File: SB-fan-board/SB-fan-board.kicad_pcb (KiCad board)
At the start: 2 copper layers, 51.6 x 35.1 mm, 15 parts, among them J1 FAN0, J2 FAN1, J3 NEO, J4 MAIN, U1 TPS54302

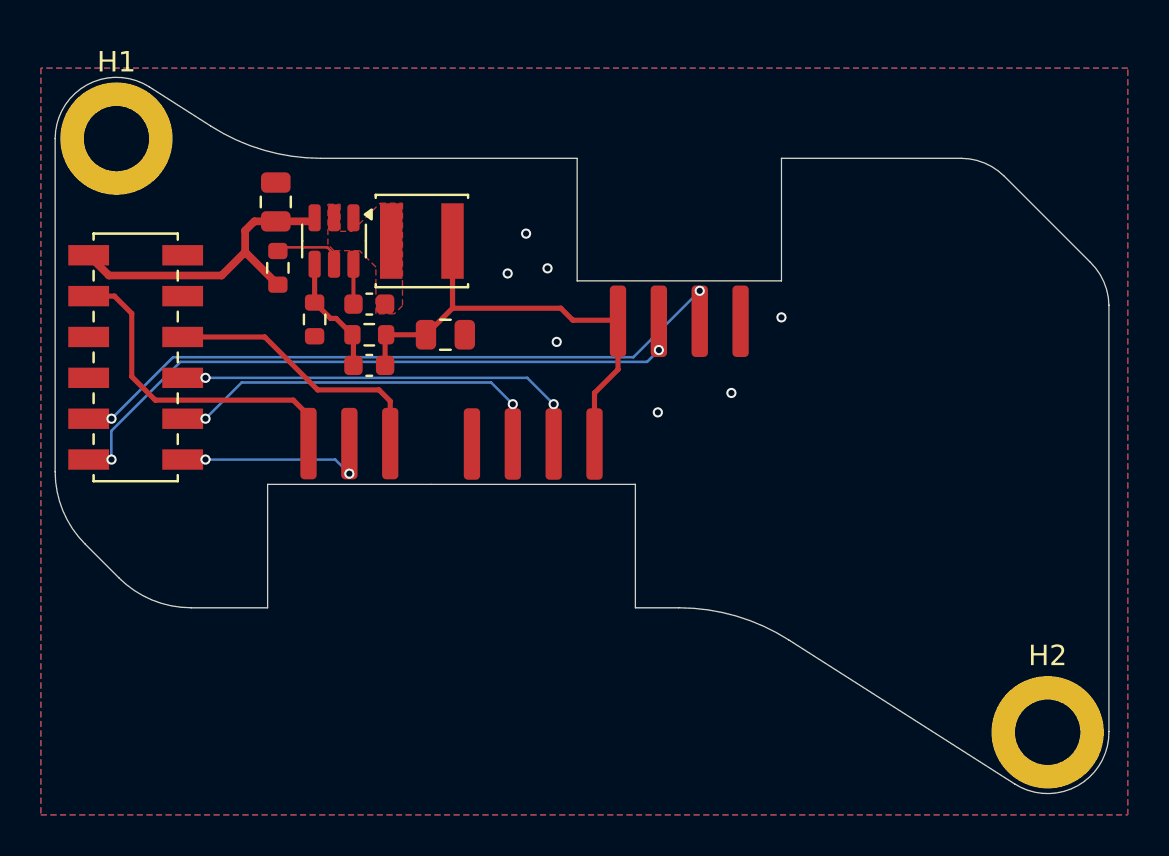
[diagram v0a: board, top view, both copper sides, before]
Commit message: mechanical: optimise installation
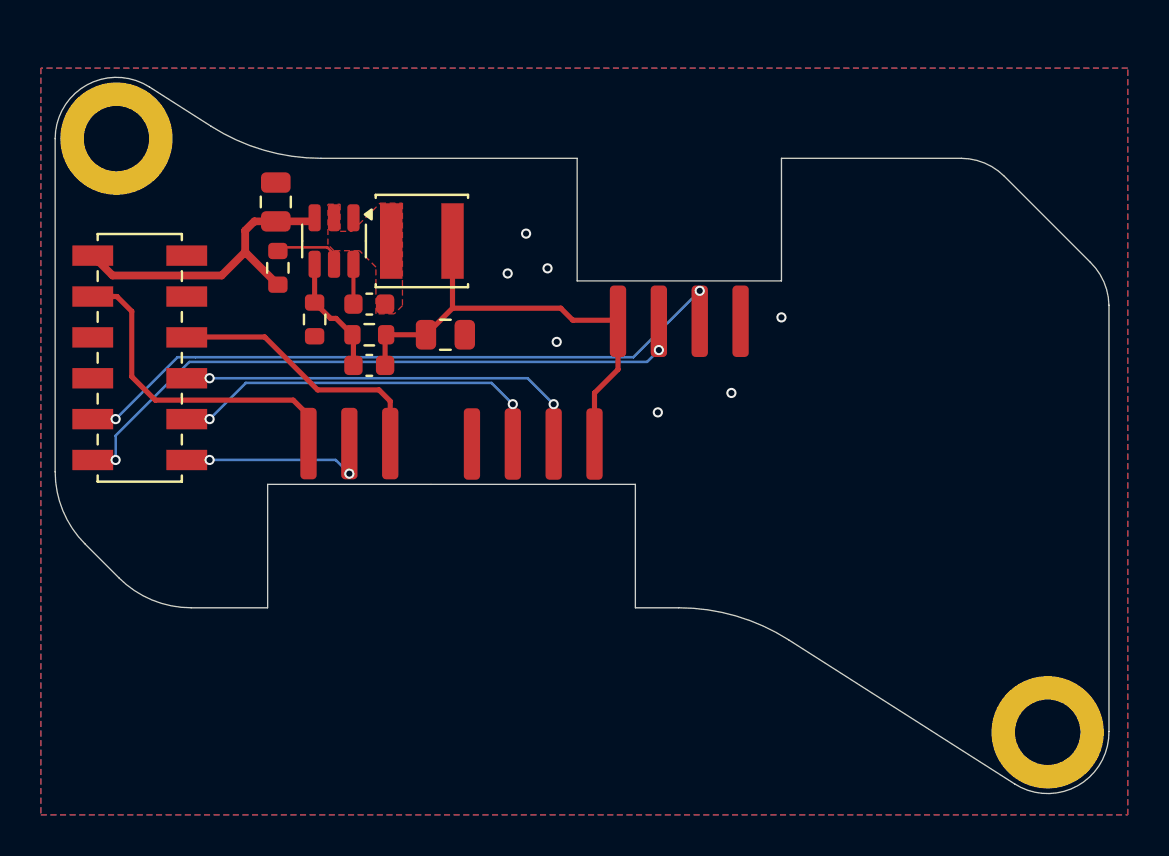
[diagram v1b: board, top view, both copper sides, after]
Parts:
- moved J4 0.20 mm to (146.3, 81.9)
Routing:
- net /FAN0_DET: track 31.0 -> 31.6 mm
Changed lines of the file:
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@@
 			(at 0 -3.75 0)
 			(layer "F.SilkS")
+			(hide yes)
 			(effects
 				(font
@@
 			(at 0 3.75 0)
 			(layer "F.Fab")
+			(hide yes)
 			(effects
 				(font
@@
 	(footprint "Library:PinSocket_2x06_P2.00mm_Vertical_SMD"
 		(layer "F.Cu")
-		(at 146.141 81.909 180)
+		(at 146.341 81.929 180)
 		(descr "surface-mounted straight socket strip, 2x06, 2.00mm pitch, double cols (from Kicad 4.0.7), script generated")
 		(tags "Surface mounted socket strip SMD 2x06 2.00mm double row")
@@
 			(at 0 -3.75 0)
 			(layer "F.SilkS")
+			(hide yes)
 			(effects
 				(font
@@
 			(at 0 3.75 0)
 			(layer "F.Fab")
+			(hide yes)
 			(effects
 				(font
@@
 	)
 	(segment
-		(start 143.841 76.909)
-		(end 144.832 77.9)
+		(start 153.1 78.35)
+		(end 151.5 76.75)
 		(width 0.381)
 		(layer "F.Cu")
@@
 	)
 	(segment
-		(start 153.1 78.35)
-		(end 151.5 76.75)
+		(start 145.012 77.9)
+		(end 150.35 77.9)
 		(width 0.381)
 		(layer "F.Cu")
@@
 	)
 	(segment
-		(start 144.832 77.9)
-		(end 150.35 77.9)
+		(start 144.041 76.929)
+		(end 145.012 77.9)
 		(width 0.381)
 		(layer "F.Cu")
@@
 	)
 	(segment
-		(start 143.841 86.909)
+		(start 144.041 86.929)
+		(end 145.159 86.929)
+		(width 0.127)
+		(layer "F.Cu")
+		(net 6)
+	)
+	(segment
+		(start 144.041 86.909)
 		(end 144.959 86.909)
 		(width 0.127)
@@
 	)
 	(via
-		(at 144.959 86.909)
+		(at 145.159 86.929)
 		(size 0.5)
 		(drill 0.3)
@@
 	)
 	(segment
-		(start 144.95 86.9)
-		(end 144.959 86.909)
-		(width 0.127)
-		(layer "B.Cu")
-		(net 6)
-	)
-	(segment
 		(start 171.75 81.55)
 		(end 171.1714 82.1286)
@@
 	)
 	(segment
-		(start 144.95 85.505041)
-		(end 144.95 86.9)
+		(start 148.7714 82.1286)
+		(end 145.159 85.741)
 		(width 0.127)
 		(layer "B.Cu")
@@
 	)
 	(segment
-		(start 148.326441 82.1286)
-		(end 144.95 85.505041)
+		(start 145.159 85.741)
+		(end 145.159 86.929)
 		(width 0.127)
 		(layer "B.Cu")
@@
 	(segment
 		(start 171.1714 82.1286)
-		(end 148.326441 82.1286)
+		(end 148.7714 82.1286)
 		(width 0.127)
 		(layer "B.Cu")
@@
 	)
 	(segment
-		(start 143.841 84.909)
-		(end 144.959 84.909)
+		(start 144.041 84.929)
+		(end 145.159 84.929)
 		(width 0.127)
 		(layer "F.Cu")
@@
 	)
 	(via
-		(at 144.959 84.909)
+		(at 145.159 84.929)
 		(size 0.5)
 		(drill 0.3)
@@
 	)
 	(segment
-		(start 144.959 84.909)
-		(end 147.968 81.9)
+		(start 149.075 81.9)
+		(end 170.5 81.9)
+		(width 0.127)
+		(layer "B.Cu")
+		(net 7)
+	)
+	(segment
+		(start 145.159 84.929)
+		(end 148.188 81.9)
 		(width 0.127)
 		(layer "B.Cu")
@@
 	)
 	(segment
-		(start 147.968 81.9)
-		(end 170.5 81.9)
+		(start 148.188 81.9)
+		(end 149.075 81.9)
 		(width 0.127)
 		(layer "B.Cu")
@@
 	)
 	(segment
-		(start 148.441 84.909)
-		(end 149.559 84.909)
+		(start 148.641 84.929)
+		(end 149.759 84.929)
 		(width 0.127)
 		(layer "F.Cu")
@@
 	)
 	(via
-		(at 149.559 84.909)
+		(at 149.759 84.929)
 		(size 0.5)
 		(drill 0.3)
@@
 	)
 	(segment
-		(start 149.559 84.909)
-		(end 151.3304 83.1376)
+		(start 151.5304 83.1576)
+		(end 163.5576 83.1576)
 		(width 0.127)
 		(layer "B.Cu")
@@
 	)
 	(segment
-		(start 163.5376 83.1376)
+		(start 163.5576 83.1576)
 		(end 164.6 84.2)
 		(width 0.127)
@@
 	)
 	(segment
-		(start 151.3304 83.1376)
-		(end 163.5376 83.1376)
+		(start 149.759 84.929)
+		(end 151.5304 83.1576)
 		(width 0.127)
 		(layer "B.Cu")
@@
 	)
 	(segment
-		(start 148.441 82.909)
-		(end 149.559 82.909)
+		(start 148.641 82.929)
+		(end 149.759 82.929)
 		(width 0.127)
 		(layer "F.Cu")
@@
 	)
 	(via
-		(at 149.559 82.909)
+		(at 149.759 82.929)
 		(size 0.5)
 		(drill 0.3)
@@
 	)
 	(segment
-		(start 149.559 82.909)
-		(end 165.309 82.909)
+		(start 165.329 82.929)
+		(end 166.6 84.2)
 		(width 0.127)
 		(layer "B.Cu")
@@
 	)
 	(segment
-		(start 165.309 82.909)
-		(end 166.6 84.2)
+		(start 149.759 82.929)
+		(end 165.329 82.929)
 		(width 0.127)
 		(layer "B.Cu")
@@
 	)
 	(segment
-		(start 148.441 86.909)
-		(end 149.559 86.909)
+		(start 148.641 86.909)
+		(end 149.759 86.909)
 		(width 0.127)
 		(layer "F.Cu")
@@
 	)
 	(via
-		(at 149.559 86.909)
+		(at 149.759 86.929)
 		(size 0.5)
 		(drill 0.3)
@@
 	)
 	(segment
-		(start 155.909 86.909)
+		(start 155.929 86.929)
 		(end 156.6 87.6)
 		(width 0.127)
@@
 	)
 	(segment
-		(start 149.559 86.909)
-		(end 155.909 86.909)
+		(start 149.759 86.929)
+		(end 155.929 86.929)
 		(width 0.127)
 		(layer "B.Cu")
@@
 	)
 	(segment
-		(start 143.841 78.909)
-		(end 145.1 78.909)
+		(start 147.1 84)
+		(end 153.854146 84)
 		(width 0.254)
 		(layer "F.Cu")
@@
 	)
 	(segment
-		(start 145.1 78.909)
-		(end 145.95 79.759)
+		(start 145.2245 78.929)
+		(end 145.95 79.6545)
 		(width 0.254)
 		(layer "F.Cu")
@@
 	)
 	(segment
-		(start 147.1 84)
-		(end 153.854146 84)
+		(start 153.854146 84)
+		(end 154.6 84.745854)
 		(width 0.254)
 		(layer "F.Cu")
@@
 	)
 	(segment
-		(start 145.95 79.759)
-		(end 145.95 82.85)
+		(start 144.041 78.929)
+		(end 145.2245 78.929)
 		(width 0.254)
 		(layer "F.Cu")
@@
 	)
 	(segment
-		(start 153.854146 84)
-		(end 154.6 84.745854)
+		(start 145.95 79.6545)
+		(end 145.95 82.85)
 		(width 0.254)
 		(layer "F.Cu")
@@
 	)
 	(segment
-		(start 158.05 83.5)
-		(end 158.6 84.05)
+		(start 148.641 80.909)
+		(end 152.459 80.909)
 		(width 0.254)
 		(layer "F.Cu")
@@
 	)
 	(segment
-		(start 155.05 83.5)
-		(end 158.05 83.5)
+		(start 158.6 84.05)
+		(end 158.6 86.197927)
 		(width 0.254)
 		(layer "F.Cu")
@@
 	)
 	(segment
-		(start 148.441 80.909)
-		(end 152.459 80.909)
+		(start 155.05 83.5)
+		(end 158.05 83.5)
 		(width 0.254)
 		(layer "F.Cu")
@@
 	)
 	(segment
-		(start 152.459 80.909)
-		(end 155.05 83.5)
+		(start 158.05 83.5)
+		(end 158.6 84.05)
 		(width 0.254)
 		(layer "F.Cu")
@@
 	)
 	(segment
-		(start 158.6 84.05)
-		(end 158.6 86.197927)
+		(start 152.459 80.909)
+		(end 155.05 83.5)
 		(width 0.254)
 		(layer "F.Cu")

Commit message: generate gerber files
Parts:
- added REF**: Voron Hex, Logos:Voron_Logo_Hex, F.Cu at (187.7, 86.3)
- added RFF**: CharlieYu, Logos:charlieyu, F.Cu at (180.9, 85.7)
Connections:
- J4 pad 5: /ADC0 -> unconnected-(J4-Pin_5-Pad5)
- J4 pad 7: /ADC1 -> unconnected-(J4-Pin_7-Pad7)
